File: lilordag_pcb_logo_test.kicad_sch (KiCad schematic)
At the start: 55 parts, among them Q1 BC846, Q2 BC846

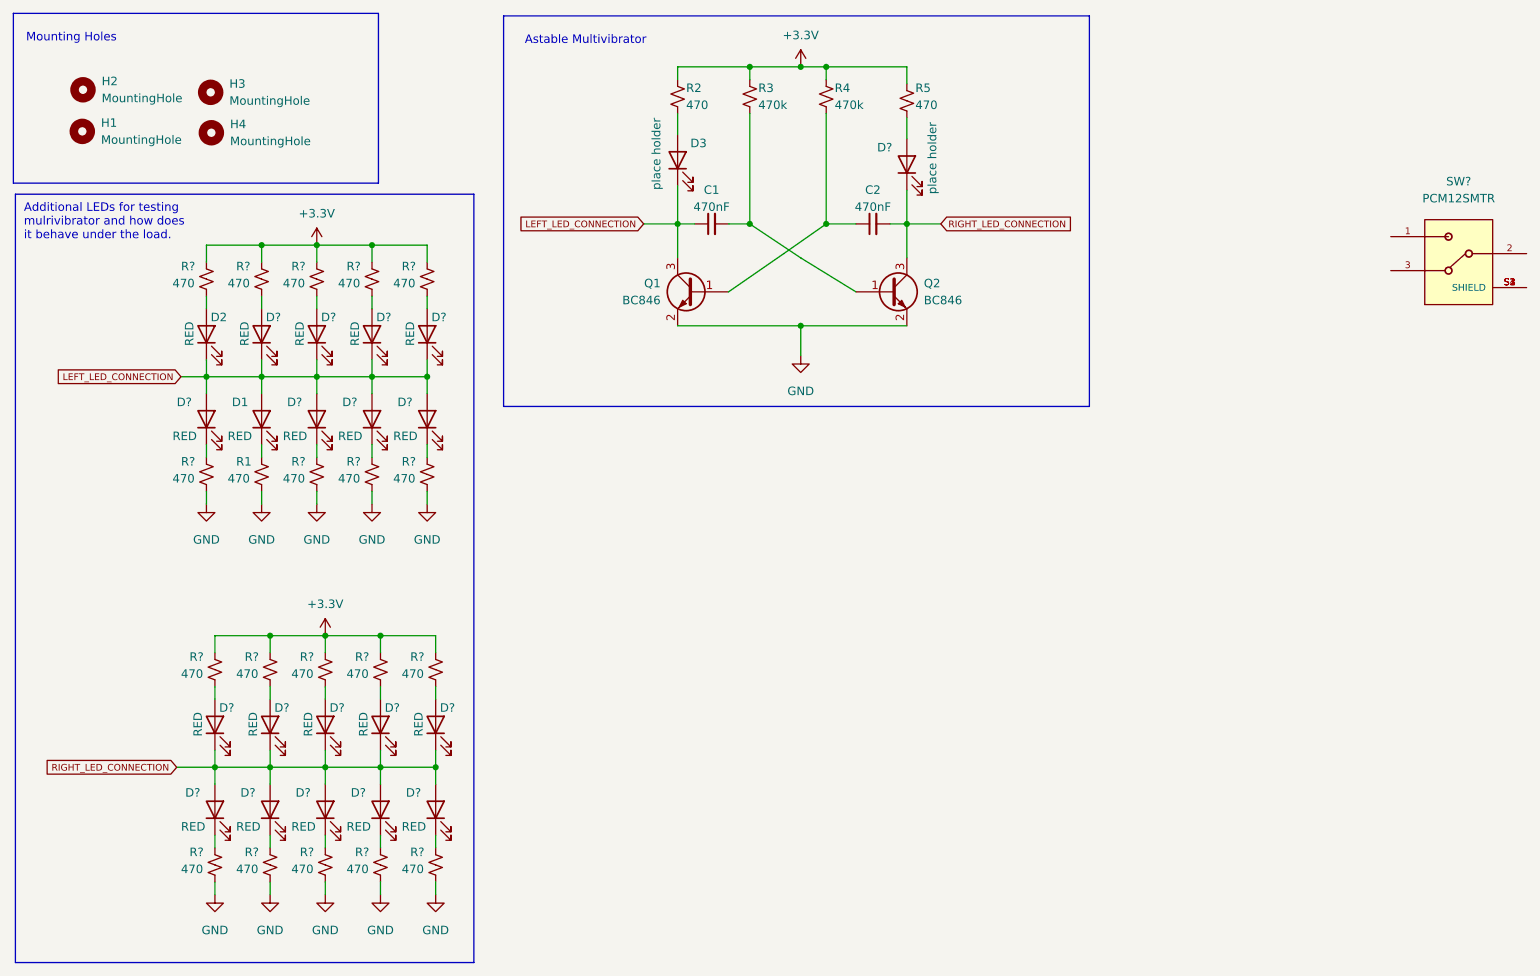
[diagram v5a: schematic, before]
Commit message: Added parts to the PCB and added 3D to switch.
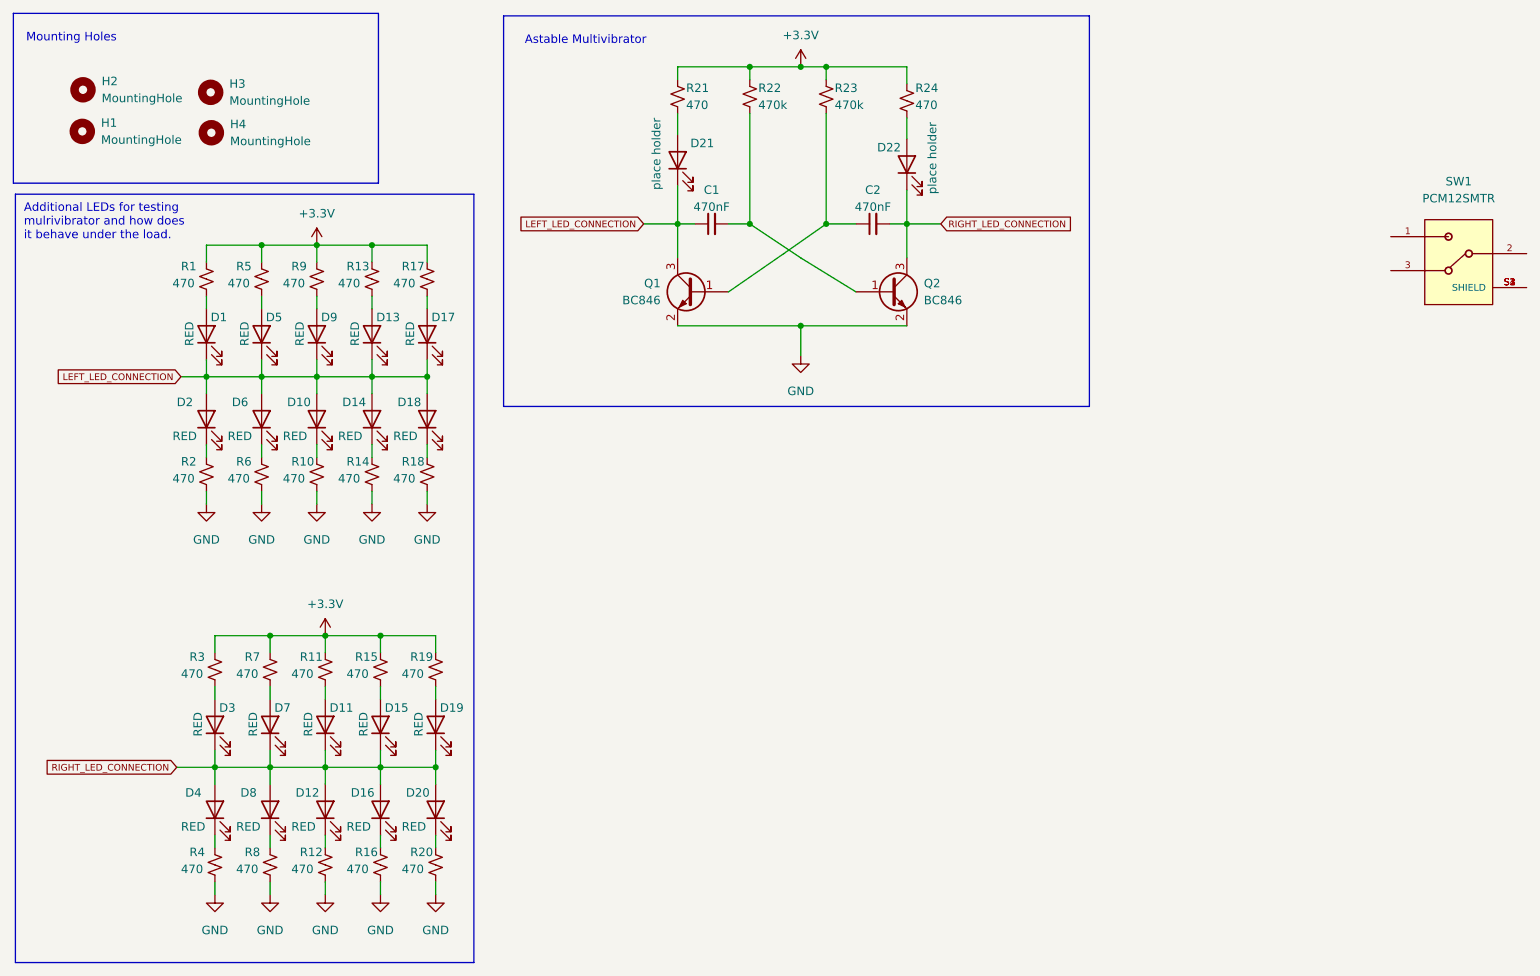
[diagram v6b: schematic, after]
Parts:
- gave numbers to parts that had none: 39
- renumbered D2 to D1, D3 to D21, D1 to D6, R2 to R21, R3 to R22, R4 to R23, R5 to R24, R1 to R6

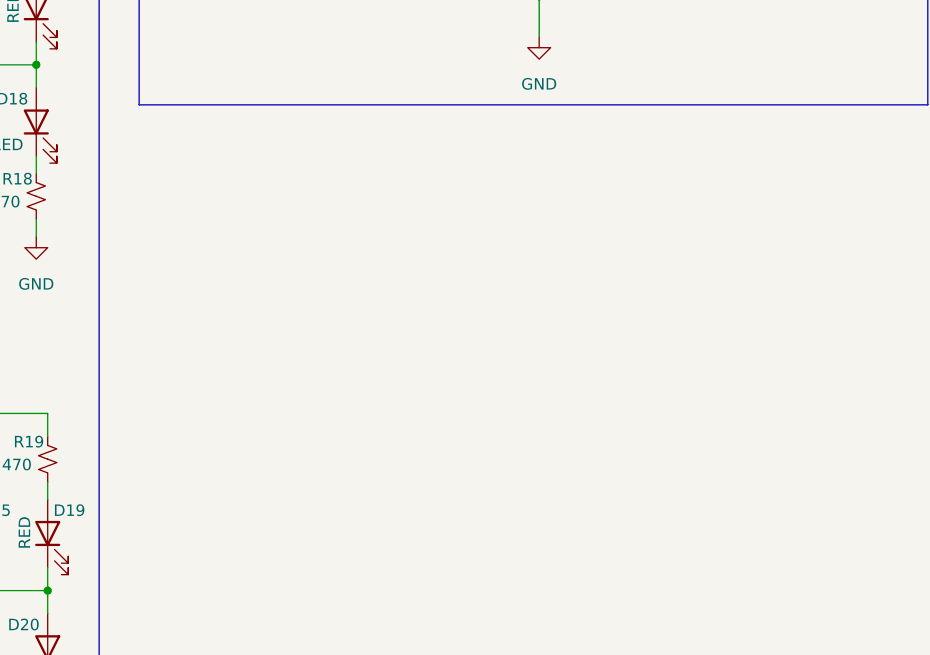
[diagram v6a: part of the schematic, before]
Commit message: Added LDO and ESP32-C3.
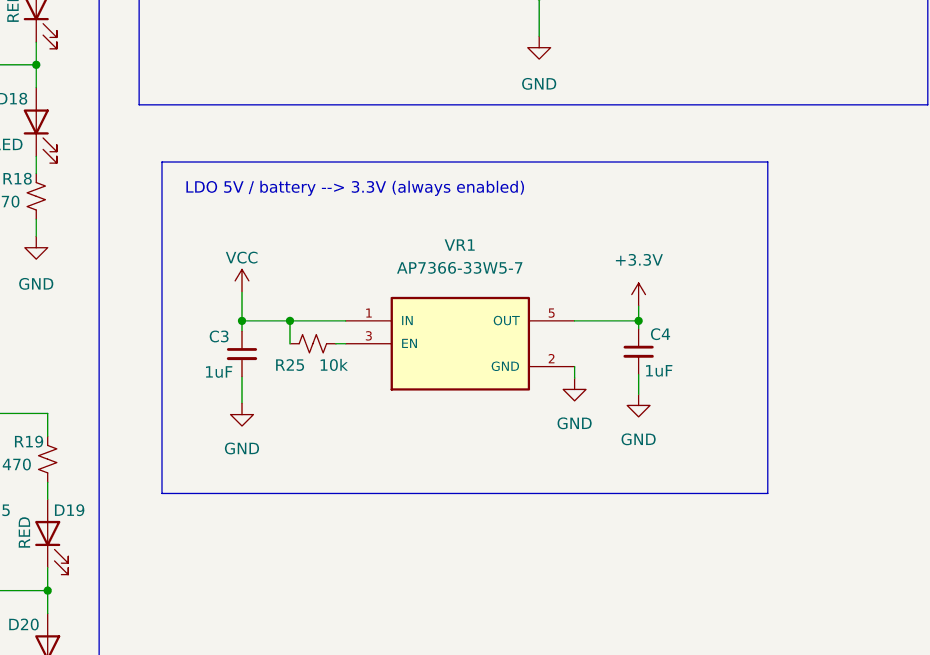
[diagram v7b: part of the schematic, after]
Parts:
- added C3, C4: 1uF, Capacitor_SMD:C_0603_1608Metric_Pad1.08x0.95mm_HandSolder, symbol Device:C_Small
- added R25: 10k, Resistor_SMD:R_0603_1608Metric_Pad0.98x0.95mm_HandSolder, symbol Device:R_Small_US
- added VR1: AP7366-33W5-7, LDO-AP7366-33W5-7:SOT95P285X140-5N, symbol AP7366-33W5-7:AP7366-33W5-7
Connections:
- net +3.3V: now also C4.1, VR1.5 (OUT)
- net GND: now also C3.2, C4.2, VR1.2 (GND)
- new net: R25.2, VR1.3 (EN)
- new net VCC: C3.1, R25.1, VR1.1 (IN)
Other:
- note added: "LDO 5V / battery --> 3.3V (always enabled)"

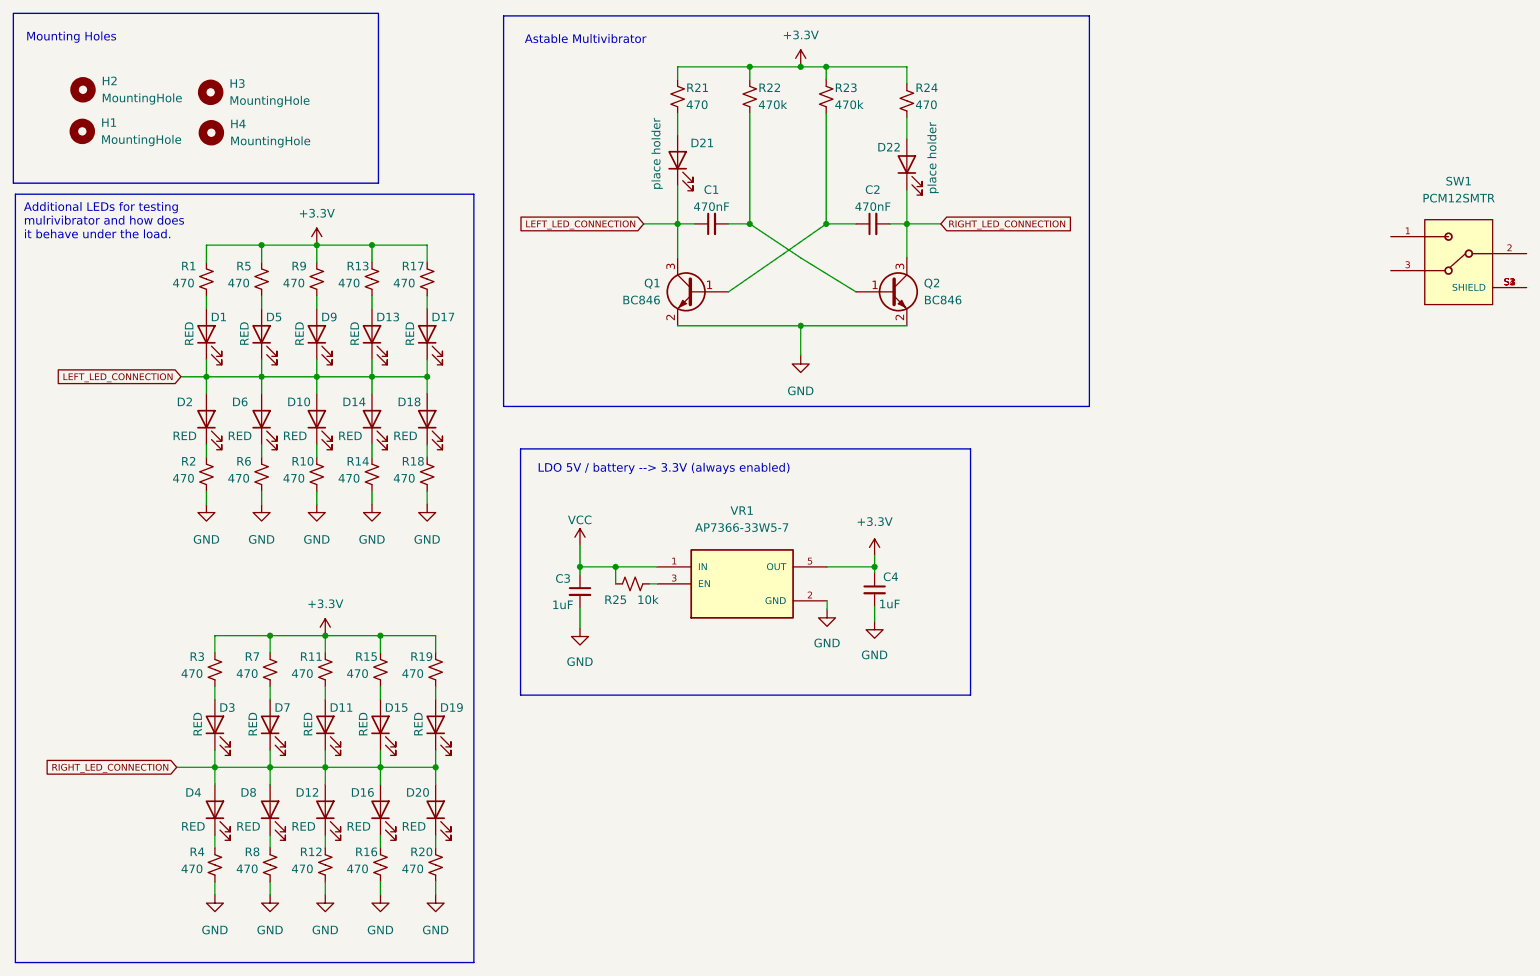
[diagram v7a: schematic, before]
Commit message: Connected the switch.
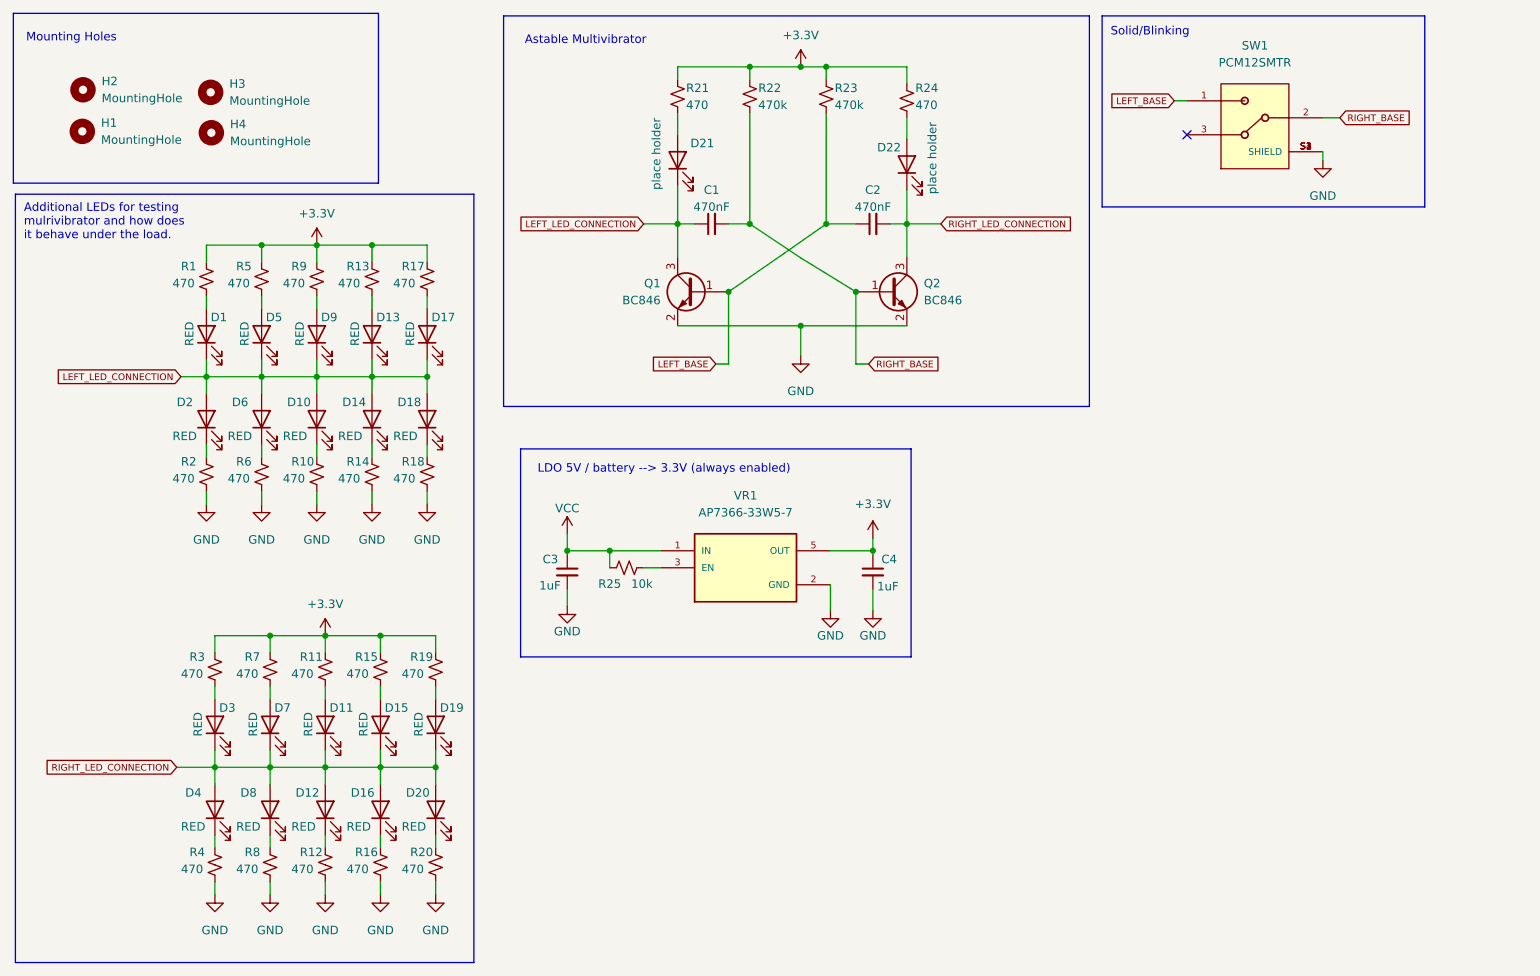
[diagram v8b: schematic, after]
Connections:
- net GND: now also SW1.S1 (SHIELD), SW1.S2 (SHIELD), SW1.S3 (SHIELD), SW1.S4 (SHIELD)
- net LEFT_BASE: now reaches C2.1, Q1.1 (B), R23.2
- net LEFT_BASE: now also SW1.1
- net RIGHT_BASE: now reaches SW1.2
- net RIGHT_BASE: now also C1.2, Q2.1 (B), R22.2
- no-connect marks 0 -> 1
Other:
- note added: "Solid/Blinking"
- moved on the sheet: C3, C4, R25, SW1
